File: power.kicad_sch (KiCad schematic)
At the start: 0 parts

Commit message: wen branch and pr
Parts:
- added C100, C55, C58, C61, C66, C70, C72, C74, C99: 100n, symbol Device:C
- added C54: 2n2, symbol Device:C
- added C56: 1u, symbol Device:C_Polarized
- added C57: 22u, symbol Device:C_Polarized
- added C59, C60, C65, C67, C76: 10u, symbol Device:C
- added C62, C63: 22u, symbol Device:C
- added C64: 10p, symbol Device:C
- added C71, C73, C75: 1u, symbol Device:C
- added D10: SMBJ51CD-M3/H, Diode_SMD:D_SMB, symbol 0_diodes:SMBJ51CD-M3/H
- added D12, D8, D9: GREEN 0402, symbol Device:LED
- added F1: 500 mA, symbol Device:Fuse
- added J4: XT30 MALE, symbol 0_connectors:Conn_01x02_Mounting
- added L2: 3u3, symbol Device:L
- added R24: 470k, 0_resistor_smd:R_0402_1005Metric, symbol Device:R
- added R25, R26, R44, R65: 39k, 0_resistor_smd:R_0402_1005Metric, symbol Device:R
- added R27: 549R, 0_resistor_smd:R_0402_1005Metric, symbol Device:R
- added R28, R29, R30: 47k, 0_resistor_smd:R_0402_1005Metric, symbol Device:R
- added R31, R32, R34, R41, R42, R64: 10k, 0_resistor_smd:R_0402_1005Metric, symbol Device:R
- added R33: 54k9, 0_resistor_smd:R_0402_1005Metric, symbol Device:R
- added R35: 3k57, 0_resistor_smd:R_0402_1005Metric, symbol Device:R
- added R36, R63: 1k15, 0_resistor_smd:R_0402_1005Metric, symbol Device:R
- added R43: 100k, 0_resistor_smd:R_0402_1005Metric, symbol Device:R
- added R45: 1k5, 0_resistor_smd:R_0402_1005Metric, symbol Device:R
- added R48: 1k, 0_resistor_smd:R_0402_1005Metric, symbol Device:R
- added R66: 10K, 0_resistor_smd:R_0402_1005Metric, symbol Device:R
- added U10: LM73100, symbol 0_power:LM73100
- added U11: TPS565201, Package_TO_SOT_SMD:SOT-23-6, symbol 0_power:TPS565201
- added U12: TPS2116DRL, Package_TO_SOT_SMD:SOT-583-8, symbol 0_power:TPS2116DRL
- added U13: TPS74801DRC, Package_SON:VSON-10-1EP_3x3mm_P0.5mm_EP1.65x2.4mm_ThermalVias, symbol 0_power:TPS74801DRC
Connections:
- new net: R25.2, R26.1, U10.2 (OVLO)
- new net: D12.2 (A), R48.2
- new net: C61.2, L2.1, U11.2 (SW)
- new net: C64.1, R32.1, R33.2, U11.4 (VFB)
- new net: R31.2, U11.5 (EN)
- new net: C61.1, U11.6 (VBST)
- new net: R28.2, R29.1, U10.4 (PGTH)
- new net: R35.1, R36.2, U13.8 (FB)
- new net: C70.2, C71.2, F1.2, U12.6 (VIN2)
- new net: C54.2, U10.7 (DVDT)
- new net: R24.2, R25.1, U10.1 (EN/UVLO)
- new net: R41.2, U12.8 (ST)
- new net: D8.2 (A), R45.2
- new net: R34.2, U13.3 (PG)
- new net: D9.2 (A), R44.2
- new net +3V3: C66.2, C67.2, R30.2, R35.2, R48.1, U13.10 (OUT), U13.9 (OUT)
- new net +5V: C65.2, C74.2, C75.2, C76.2, R34.1, R41.1, R45.1, R65.2, U12.2 (VOUT), U12.7 (VOUT), U13.1 (IN), U13.2 (IN), U13.4 (BIAS), U13.5 (EN)
- new net +5V_EXT: C62.2, C63.2, C64.2, C72.2, C73.2, L2.2, R33.1, R42.1, U12.3 (VIN1), U12.5 (MODE)
- new net +BAT: C56.1, D10.1 (A1), J4.2 (Pin_2), R24.1, U10.5 (VIN)
- new net +BAT_PROT: C57.1, C58.2, C59.2, C60.2, R28.1, R31.1, R44.1, R63.2, U10.6 (VOUT), U11.3 (VIN)
- new net +BAT_VMON: C100.2, C99.2, R63.1, R64.2, R65.1, R66.2
- new net +VBUS: F1.1
- new net BATTERY_IMON: C55.2, R27.1, U10.9 (IMON)
- new net BAT_PG: R30.1, U10.3 (PG)
- new net GND: C100.1, C54.1, C55.1, C56.2, C57.2, C58.1, C59.1, C60.1, C62.1, C63.1, C65.1, C66.1, C67.1, C70.1, C71.1, C72.1, C73.1, C74.1, C75.1, C76.1, C99.1, D10.2 (A2), D12.1 (K), D8.1 (K), D9.1 (K), J4.1 (Pin_1), J4.MP1, J4.MP2, R26.2, R27.2, R29.2, R32.2, R36.1, R43.2, R64.1, R66.1, U10.8 (GND), U11.1 (GND), U12.1 (GND), U13.11 (GND), U13.6 (GND)
- new net MUX_PR1: R42.2, R43.1, U12.4 (PR1)
- no-connect marks 0 -> 2
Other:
- note added: "3V3 @ 1.5A LDO"
- note added: "5V @ 2.5A MUX (USB & 5V BUCK)"
- note added: "5V @ 5A BUCK"
- note added: "BATTERY INPUT IDEAL DIODE"
- note added: "PWR LEDs"
- note added: "VOLTAGE MONITORING"
- note added: "XT30 POWER CONNECTOR"
- title: (none) -> POWER

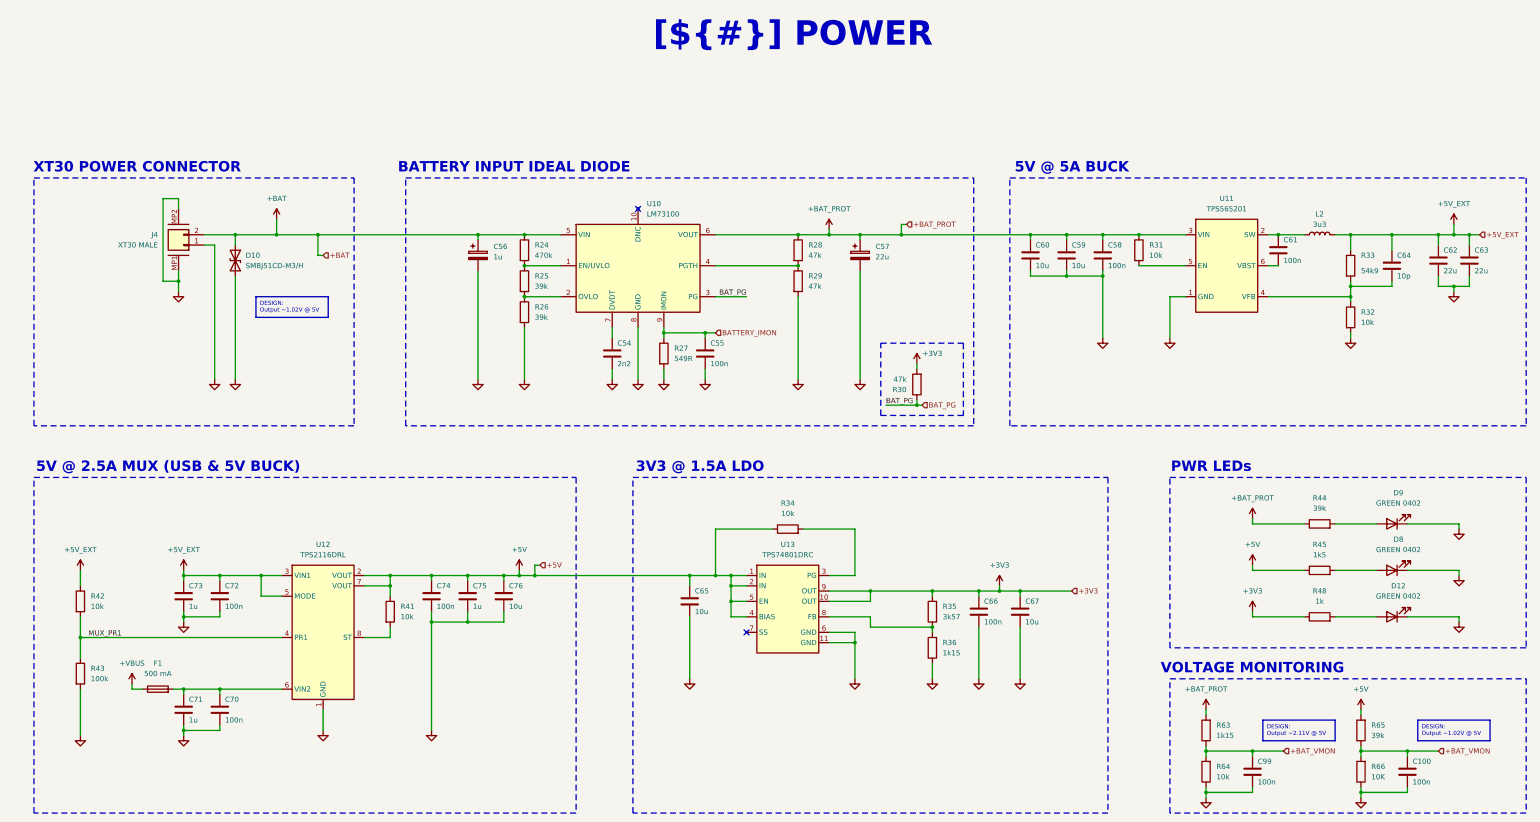
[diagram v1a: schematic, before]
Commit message: much work and .ioc file added
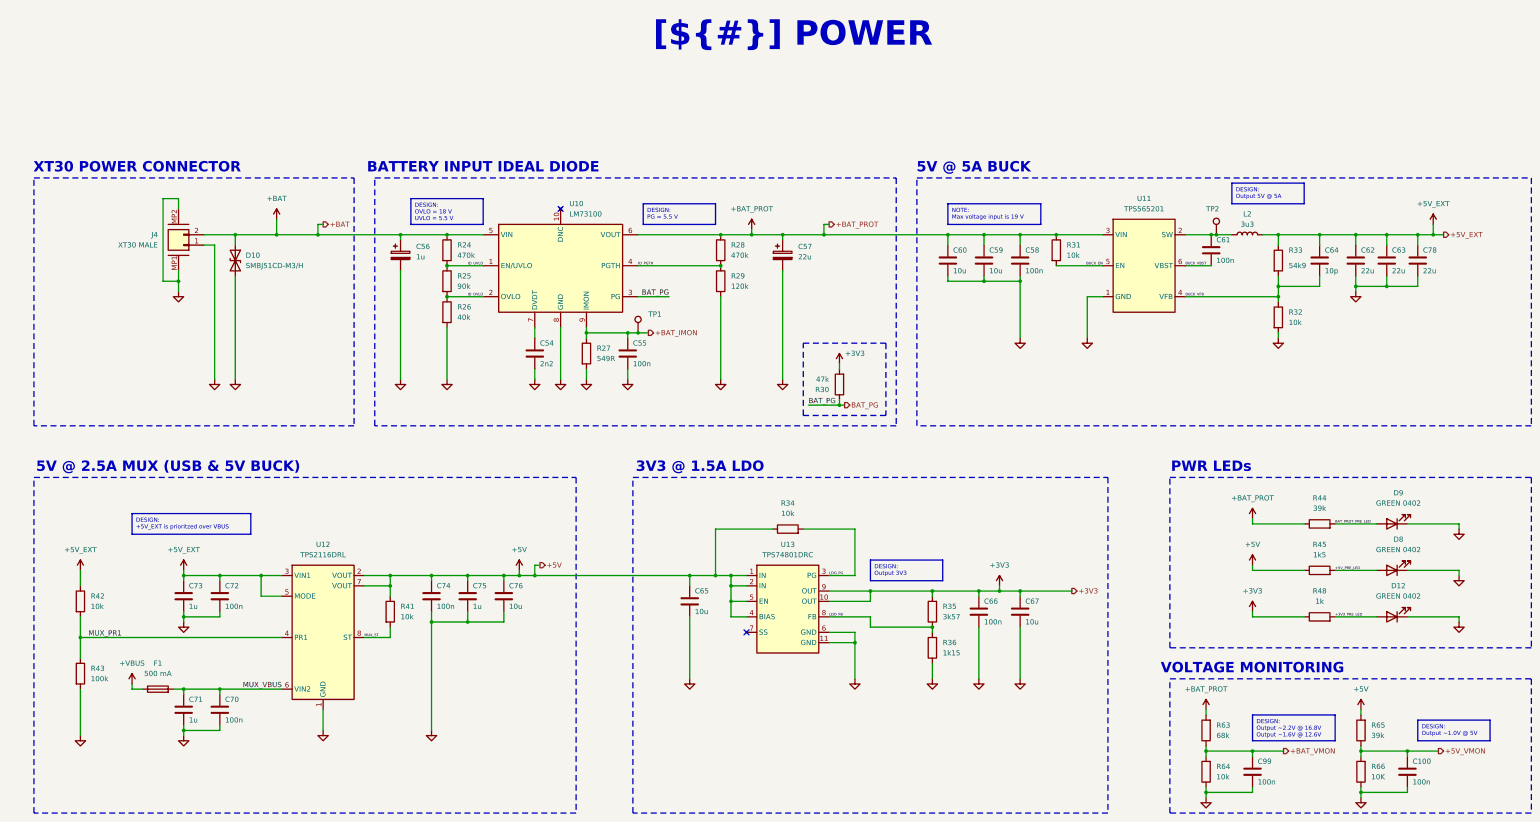
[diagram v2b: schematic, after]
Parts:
- added C78: 22u, symbol Device:C
- added TP1, TP2: TestPoint, symbol Connector:TestPoint
- R25: value 39k -> 90k
- R26: value 39k -> 40k
- R28: value 47k -> 470k
- R29: value 47k -> 120k
- R63: value 1k15 -> 68k
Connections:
- net +5V_EXT: now also C78.2
- net +BAT_VMON: no longer C100.2, R65.1, R66.2
- net GND: now also C78.1
- net ID_OVLO: now reaches R25.2, R26.1, U10.2 (OVLO)
- net +3V3_PRE_LED: now reaches D12.2 (A), R48.2
- net at C61.2, L2.1, U11.2 (SW): now also TP2.1
- net BUCK_VFB: now reaches C64.1, R32.1, R33.2, U11.4 (VFB)
- net BUCK_EN: now reaches R31.2, U11.5 (EN)
- net BUCK_VBST: now reaches C61.1, U11.6 (VBST)
- net ID_PGTH: now reaches R28.2, R29.1, U10.4 (PGTH)
- net LDO_FB: now reaches R35.1, R36.2, U13.8 (FB)
- net MUX_VBUS: now reaches C70.2, C71.2, F1.2, U12.6 (VIN2)
- net ID_UVLO: now reaches R24.2, R25.1, U10.1 (EN/UVLO)
- net MUX_ST: now reaches R41.2, U12.8 (ST)
- net +5V_PRE_LED: now reaches D8.2 (A), R45.2
- net LDO_PG: now reaches R34.2, U13.3 (PG)
- net BAT_PROT_PRE_LED: now reaches D9.2 (A), R44.2
- net BATTERY_IMON renamed +BAT_IMON
- net +BAT_IMON: now also TP1.1
- new net +5V_VMON: C100.2, R65.1, R66.2
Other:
- moved on the sheet: C54, C55, C56, C57, C58, C59, C60, C61, C62, C63, C64, L2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
